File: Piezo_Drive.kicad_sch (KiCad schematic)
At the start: 79 parts, among them IC2 TMUX7219DGKRQ1, J26 SJ1-3514-SMT-TR, J32 SMA, J33 Conn_01x04, Q1 MMBT3906, Q2 mmbt3904, Q3 2SCR573, Q4 2SAR573, Q5 MMBT3906, Q6 mmbt3904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

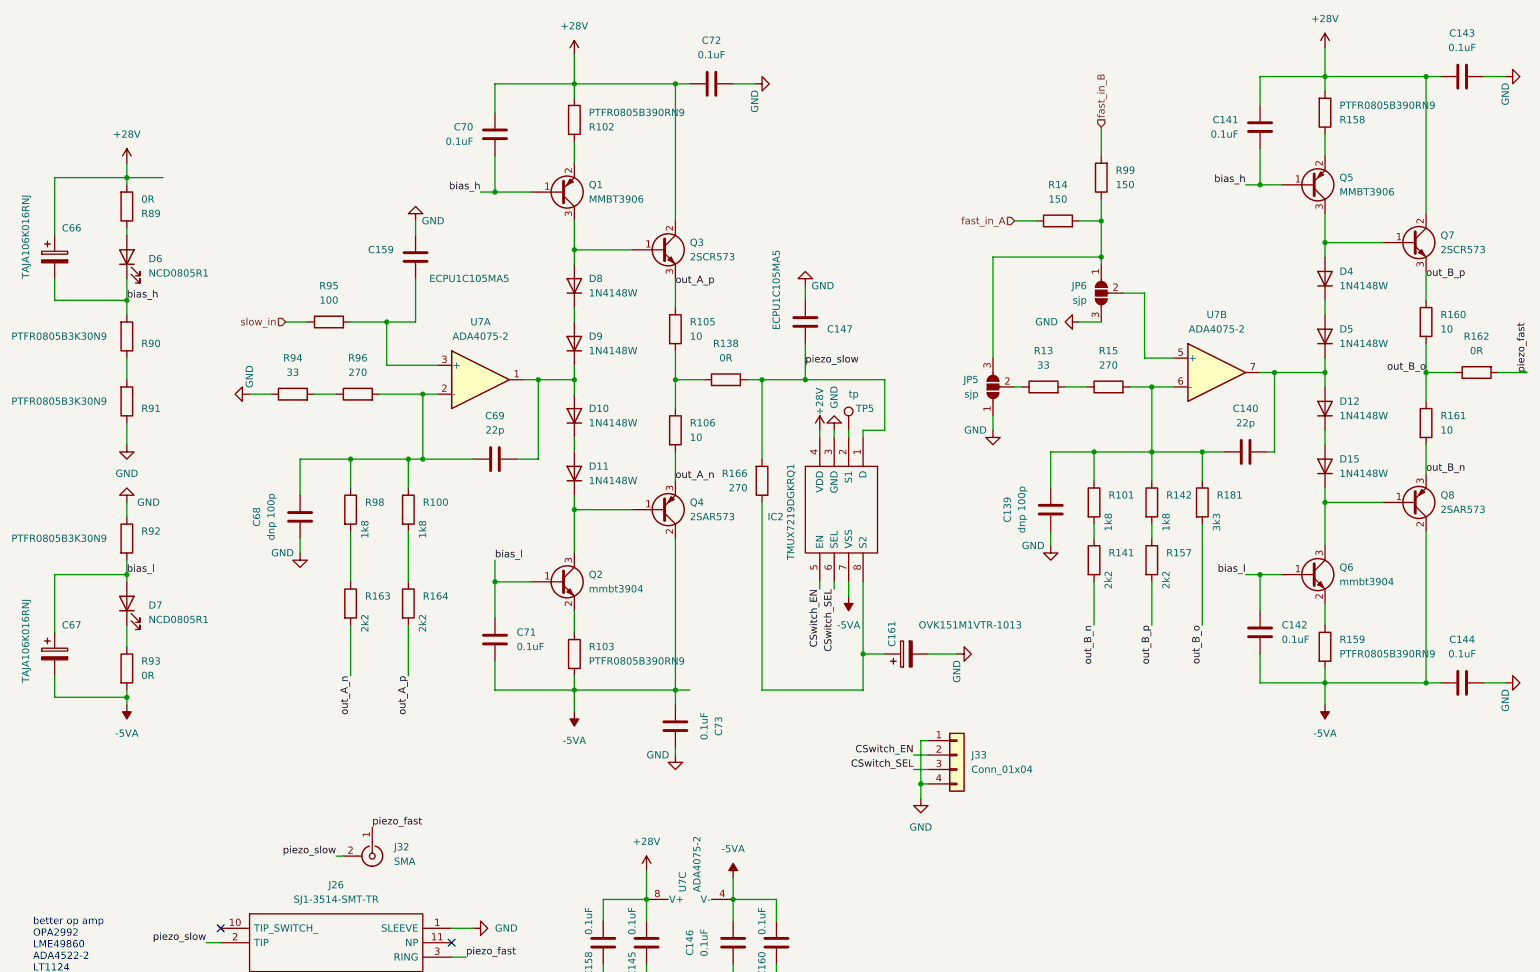
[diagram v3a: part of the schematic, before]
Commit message: Version 1.0 submitted to JLCPCB
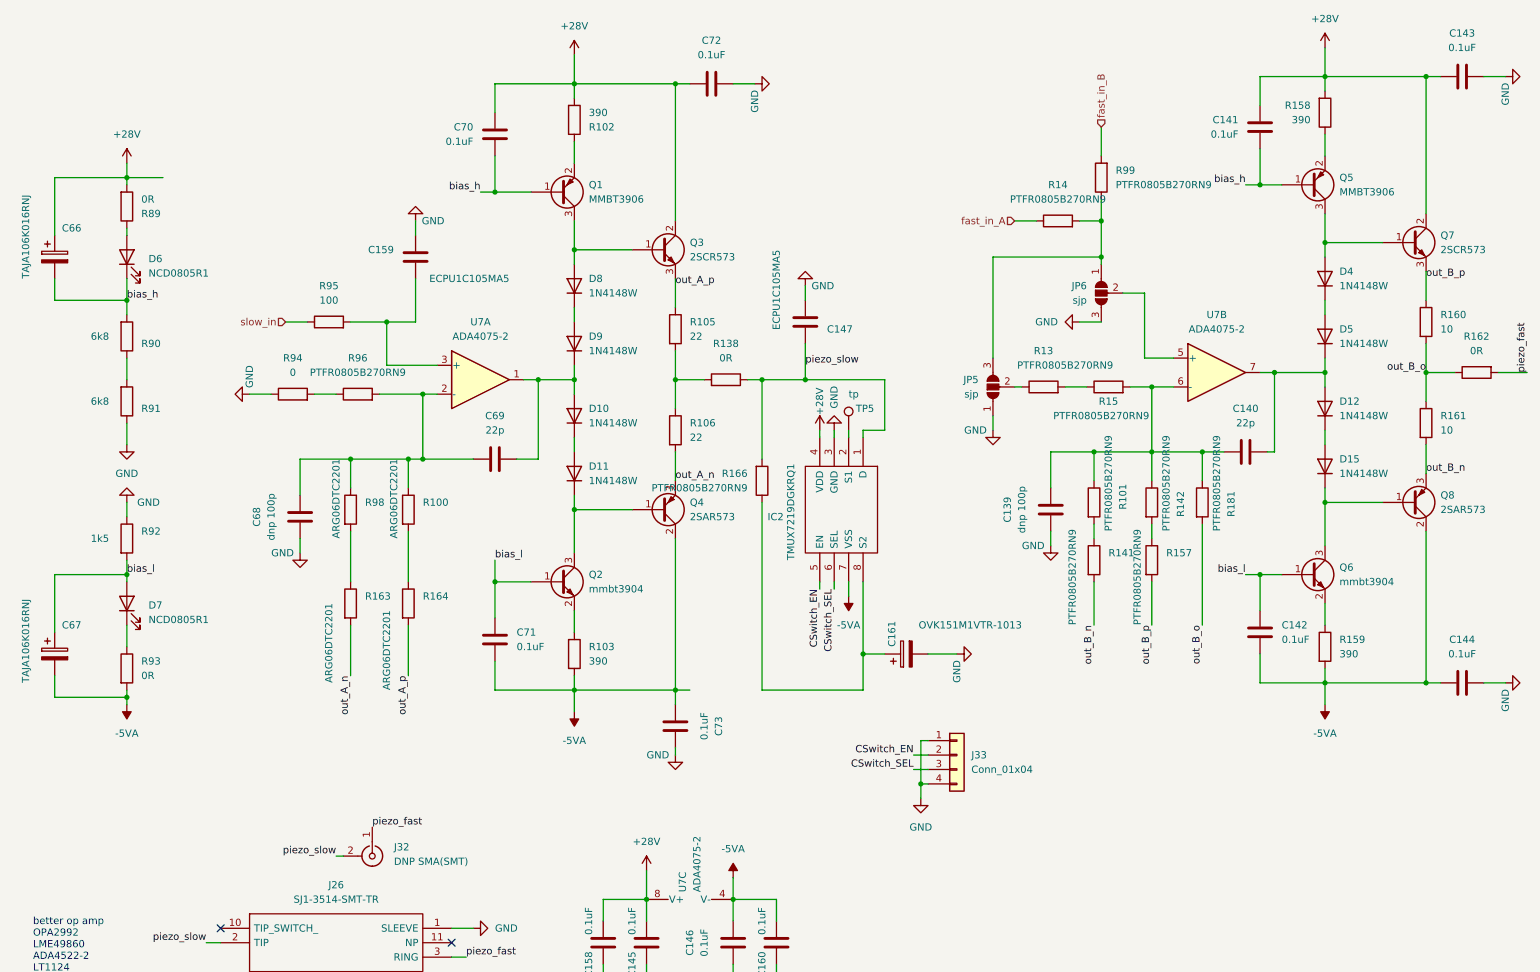
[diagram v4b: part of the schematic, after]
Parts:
- J32: value SMA -> DNP SMA(SMT)
- R100, R98: value 1k8 -> ARG06DTC2201
- R101, R142: value 1k8 -> PTFR0805B270RN9
- R102, R103, R158, R159: value PTFR0805B390RN9 -> 390
- R105, R106: value 10 -> 22
- R13: value 33 -> PTFR0805B270RN9
- R14, R99: value 150 -> PTFR0805B270RN9
- R141, R157: value 2k2 -> PTFR0805B270RN9
- R15, R166, R96: value 270 -> PTFR0805B270RN9
- R163, R164: value 2k2 -> ARG06DTC2201
- R181: value 3k3 -> PTFR0805B270RN9
- R90, R91: value PTFR0805B3K30N9 -> 6k8
- R92: value PTFR0805B3K30N9 -> 1k5
- R94: value 33 -> 0
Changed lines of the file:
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@@
       (effects (font (size 1.27 1.27)) (justify left))
     )
-    (property "Value" "SMA" (id 1) (at 80.01 164.7824 90)
+    (property "Value" "DNP SMA(SMT)" (id 1) (at 80.01 164.7824 90)
       (effects (font (size 1.27 1.27)) (justify left))
     )
@@
   (symbol (lib_id "Device:R") (at 243.84 33.02 0) (mirror x) (unit 1)
     (in_bom yes) (on_board yes) (fields_autoplaced)
-    (property "Reference" "R158" (id 0) (at 246.38 34.2901 0)
-      (effects (font (size 1.27 1.27)) (justify left))
-    )
-    (property "Value" "PTFR0805B390RN9" (id 1) (at 246.38 31.7501 0)
-      (effects (font (size 1.27 1.27)) (justify left))
+    (property "Reference" "R158" (id 0) (at 241.3 31.7499 0)
+      (effects (font (size 1.27 1.27)) (justify right))
+    )
+    (property "Value" "390" (id 1) (at 241.3 34.2899 0)
+      (effects (font (size 1.27 1.27)) (justify right))
     )
     (property "Footprint" "Resistor_SMD:R_0805_2012Metric" (id 2) (at 242.062 33.02 90)
@@
       (effects (font (size 1.27 1.27)) (justify left))
     )
-    (property "Value" "10" (id 1) (at 132.08 90.1699 0)
+    (property "Value" "22" (id 1) (at 132.08 90.1699 0)
       (effects (font (size 1.27 1.27)) (justify left))
     )
@@
       (effects (font (size 1.27 1.27)) (justify left))
     )
-    (property "Value" "PTFR0805B390RN9" (id 1) (at 114.3 33.0201 0)
+    (property "Value" "390" (id 1) (at 114.3 33.0201 0)
       (effects (font (size 1.27 1.27)) (justify left))
     )
@@
   (symbol (lib_id "Device:R") (at 222.25 101.6 0) (unit 1)
     (in_bom yes) (on_board yes)
-    (property "Reference" "R181" (id 0) (at 224.79 100.3299 0)
-      (effects (font (size 1.27 1.27)) (justify left))
-    )
-    (property "Value" "3k3" (id 1) (at 224.79 106.68 90)
+    (property "Reference" "R181" (id 0) (at 227.33 104.14 90)
+      (effects (font (size 1.27 1.27)) (justify left))
+    )
+    (property "Value" "PTFR0805B270RN9" (id 1) (at 224.79 106.68 90)
       (effects (font (size 1.27 1.27)) (justify left))
     )
@@
       (effects (font (size 1.27 1.27)) (justify left))
     )
-    (property "Value" "2k2" (id 1) (at 74.93 124.46 90)
+    (property "Value" "ARG06DTC2201" (id 1) (at 68.58 133.35 90)
       (effects (font (size 1.27 1.27)) (justify left))
     )
@@
       (effects (font (size 1.27 1.27)) (justify left))
     )
-    (property "Value" "PTFR0805B390RN9" (id 1) (at 246.38 128.2699 0)
+    (property "Value" "390" (id 1) (at 246.38 128.2699 0)
       (effects (font (size 1.27 1.27)) (justify left))
     )
@@
       (effects (font (size 1.27 1.27)) (justify right))
     )
-    (property "Value" "270" (id 1) (at 142.24 99.0599 0)
+    (property "Value" "PTFR0805B270RN9" (id 1) (at 142.24 99.0599 0)
       (effects (font (size 1.27 1.27)) (justify right))
     )
@@
   )
   (symbol (lib_id "Device:R") (at 194.31 81.28 90) (unit 1)
-    (in_bom yes) (on_board yes) (fields_autoplaced)
+    (in_bom yes) (on_board yes)
     (property "Reference" "R13" (id 0) (at 194.31 74.93 90))
-    (property "Value" "33" (id 1) (at 194.31 77.47 90))
+    (property "Value" "PTFR0805B270RN9" (id 1) (at 198.12 77.47 90))
     (property "Footprint" "Resistor_SMD:R_0805_2012Metric" (id 2) (at 194.31 83.058 90)
       (effects (font (size 1.27 1.27)) hide)
@@
     (in_bom yes) (on_board yes)
     (property "Reference" "R96" (id 0) (at 73.66 76.2 90))
-    (property "Value" "270" (id 1) (at 73.66 78.74 90))
+    (property "Value" "PTFR0805B270RN9" (id 1) (at 73.66 78.74 90))
     (property "Footprint" "Resistor_SMD:R_0805_2012Metric" (id 2) (at 73.66 84.328 90)
       (effects (font (size 1.27 1.27)) hide)
@@
       (effects (font (size 1.27 1.27)) (justify left))
     )
-    (property "Value" "10" (id 1) (at 132.08 72.3899 0)
+    (property "Value" "22" (id 1) (at 132.08 72.3899 0)
       (effects (font (size 1.27 1.27)) (justify left))
     )
@@
       (effects (font (size 1.27 1.27)) (justify left))
     )
-    (property "Value" "2k2" (id 1) (at 205.74 116.84 90)
+    (property "Value" "PTFR0805B270RN9" (id 1) (at 199.39 123.19 90)
       (effects (font (size 1.27 1.27)) (justify left))
     )
@@
       (effects (font (size 1.27 1.27)) (justify left))
     )
-    (property "Value" "PTFR0805B3K30N9" (id 1) (at 12.7 83.82 0)
+    (property "Value" "6k8" (id 1) (at 26.67 83.82 0)
       (effects (font (size 1.27 1.27)) (justify left))
     )
@@
   (symbol (lib_id "Device:R") (at 203.2 101.6 0) (unit 1)
     (in_bom yes) (on_board yes)
-    (property "Reference" "R101" (id 0) (at 205.74 100.3299 0)
-      (effects (font (size 1.27 1.27)) (justify left))
-    )
-    (property "Value" "1k8" (id 1) (at 205.74 106.68 90)
+    (property "Reference" "R101" (id 0) (at 208.28 102.87 90)
+      (effects (font (size 1.27 1.27)) (justify left))
+    )
+    (property "Value" "PTFR0805B270RN9" (id 1) (at 205.74 106.68 90)
       (effects (font (size 1.27 1.27)) (justify left))
     )
@@
       (effects (font (size 1.27 1.27)) (justify left))
     )
-    (property "Value" "2k2" (id 1) (at 85.09 124.46 90)
+    (property "Value" "ARG06DTC2201" (id 1) (at 78.74 134.62 90)
       (effects (font (size 1.27 1.27)) (justify left))
     )
@@
   (symbol (lib_id "Device:R") (at 205.74 81.28 90) (unit 1)
     (in_bom yes) (on_board yes)
-    (property "Reference" "R15" (id 0) (at 205.74 74.93 90))
-    (property "Value" "270" (id 1) (at 205.74 77.47 90))
+    (property "Reference" "R15" (id 0) (at 205.74 83.82 90))
+    (property "Value" "PTFR0805B270RN9" (id 1) (at 204.47 86.36 90))
     (property "Footprint" "Resistor_SMD:R_0805_2012Metric" (id 2) (at 205.74 83.058 90)
       (effects (font (size 1.27 1.27)) hide)
@@
       (effects (font (size 1.27 1.27)) (justify left))
     )
-    (property "Value" "PTFR0805B390RN9" (id 1) (at 114.3 129.5399 0)
+    (property "Value" "390" (id 1) (at 114.3 129.5399 0)
       (effects (font (size 1.27 1.27)) (justify left))
     )
@@
       (effects (font (size 1.27 1.27)) (justify left))
     )
-    (property "Value" "2k2" (id 1) (at 215.9 116.84 90)
+    (property "Value" "PTFR0805B270RN9" (id 1) (at 210.82 123.19 90)
       (effects (font (size 1.27 1.27)) (justify left))
     )
@@
       (effects (font (size 1.27 1.27)) (justify left))
     )
-    (property "Value" "PTFR0805B3K30N9" (id 1) (at 12.7 107.95 0)
+    (property "Value" "1k5" (id 1) (at 26.67 107.95 0)
       (effects (font (size 1.27 1.27)) (justify left))
     )
@@
       (effects (font (size 1.27 1.27)) (justify left))
     )
-    (property "Value" "PTFR0805B3K30N9" (id 1) (at 12.7 72.39 0)
+    (property "Value" "6k8" (id 1) (at 26.67 72.39 0)
       (effects (font (size 1.27 1.27)) (justify left))
     )
@@
       (effects (font (size 1.27 1.27)) (justify right))
     )
-    (property "Value" "150" (id 1) (at 207.01 45.7199 0)
+    (property "Value" "PTFR0805B270RN9" (id 1) (at 207.01 45.7199 0)
       (effects (font (size 1.27 1.27)) (justify right))
     )
@@
       (effects (font (size 1.27 1.27)) (justify left))
     )
-    (property "Value" "1k8" (id 1) (at 85.09 107.95 90)
+    (property "Value" "ARG06DTC2201" (id 1) (at 80.01 107.95 90)
       (effects (font (size 1.27 1.27)) (justify left))
     )
@@
   (symbol (lib_id "Device:R") (at 213.36 101.6 0) (unit 1)
     (in_bom yes) (on_board yes)
-    (property "Reference" "R142" (id 0) (at 215.9 100.3299 0)
-      (effects (font (size 1.27 1.27)) (justify left))
-    )
-    (property "Value" "1k8" (id 1) (at 215.9 106.68 90)
+    (property "Reference" "R142" (id 0) (at 218.44 104.14 90)
+      (effects (font (size 1.27 1.27)) (justify left))
+    )
+    (property "Value" "PTFR0805B270RN9" (id 1) (at 215.9 106.68 90)
       (effects (font (size 1.27 1.27)) (justify left))
     )
@@
       (effects (font (size 1.27 1.27)) (justify left))
     )
-    (property "Value" "1k8" (id 1) (at 74.93 107.95 90)
+    (property "Value" "ARG06DTC2201" (id 1) (at 69.85 107.95 90)
       (effects (font (size 1.27 1.27)) (justify left))
     )
@@
     (in_bom yes) (on_board yes) (fields_autoplaced)
     (property "Reference" "R94" (id 0) (at 62.23 76.2 90))
-    (property "Value" "33" (id 1) (at 62.23 78.74 90))
+    (property "Value" "0" (id 1) (at 62.23 78.74 90))
     (property "Footprint" "Resistor_SMD:R_0805_2012Metric" (id 2) (at 62.23 84.328 90)
       (effects (font (size 1.27 1.27)) hide)
@@
     (in_bom yes) (on_board yes) (fields_autoplaced)
     (property "Reference" "R14" (id 0) (at 196.85 45.72 90))
-    (property "Value" "150" (id 1) (at 196.85 48.26 90))
+    (property "Value" "PTFR0805B270RN9" (id 1) (at 196.85 48.26 90))
     (property "Footprint" "Resistor_SMD:R_0805_2012Metric" (id 2) (at 196.85 53.848 90)
       (effects (font (size 1.27 1.27)) hide)
